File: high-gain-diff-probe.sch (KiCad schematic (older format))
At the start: 106 parts, among them J1 30V DC IN, J2 BNC, J4 BNC, J5 BNC, K1 FTR-B3SA012Z, K2 FTR-B3SA012Z, Q1 MMBT3906, SW1 MB04L1NCGD, SW2 MB05L1NCGD, SW3 SPDT, SW4 MB04L1NCGD, SW6 SPDT, U1 AD8428BRZ, U2 OP1177AR, U3 BUF634A, U6 LM393, U7 AD8671, U8 BUF634A

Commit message: Use larger thermal vias for cheaper PCBs
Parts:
- U3, U8: footprint Package_SO:SOIC-8-1EP_3.9x4.9mm_P1.27mm_EP2.41x3.81mm_ThermalVias -> high-gain-diff-probe:SOIC-8-1EP_3.9x4.9mm_P1.27mm_EP2.41x3.81mm_LargeThermalVias
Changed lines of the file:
@@
 F 0 "U3" H 14450 2550 50  0000 L CNN
 F 1 "BUF634A" H 14450 2150 50  0000 L CNN
-F 2 "Package_SO:SOIC-8-1EP_3.9x4.9mm_P1.27mm_EP2.41x3.81mm_ThermalVias" H 14350 2050 50  0001 C CNN
+F 2 "high-gain-diff-probe:SOIC-8-1EP_3.9x4.9mm_P1.27mm_EP2.41x3.81mm_LargeThermalVias" H 14350 2050 50  0001 C CNN
 F 3 "https://www.ti.com/lit/ds/symlink/buf634a.pdf?ts=1618584295467&ref_url=https%253A%252F%252Fcz.mouser.com%252F" H 14350 2350 50  0001 C CNN
 	1    14350 2350
@@
 F 0 "U8" H 4000 9150 50  0000 L CNN
 F 1 "BUF634A" H 4000 8850 50  0000 L CNN
-F 2 "Package_SO:SOIC-8-1EP_3.9x4.9mm_P1.27mm_EP2.41x3.81mm_ThermalVias" H 3950 8700 50  0001 C CNN
+F 2 "high-gain-diff-probe:SOIC-8-1EP_3.9x4.9mm_P1.27mm_EP2.41x3.81mm_LargeThermalVias" H 3950 8700 50  0001 C CNN
 F 3 "https://www.ti.com/lit/ds/symlink/buf634a.pdf?ts=1618584295467&ref_url=https%253A%252F%252Fcz.mouser.com%252F" H 3950 9000 50  0001 C CNN
 	1    3950 9000

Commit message: Add MPNs for everything else
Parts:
- D1, D2, D3: MPN (none) -> BAV199,215
- D17: value LED -> RED LED; footprint LED_THT:LED_D3.0mm -> LED_THT:LED_D5.0mm; MPN (none) -> MT4118-HR-A
- F4: value 1A Fast -> 500mA Fast; MPN (none) -> F0805B0R50FWTR
- J1: MPN (none) -> PJ-063AH
- J2, J4, J5: MPN (none) -> 0731385033
- Q1: MPN (none) -> MMBT3906-TP
- R10, R4, R5, R9: MPN (none) -> RT0603BRD071ML
- R13, R30: MPN (none) -> RMCF0603FT200R
- R14: MPN (none) -> CR0603-FX-1001ELF
- R15, R21: MPN (none) -> RT0603FRE07100KL
- R16: MPN (none) -> RMCF1210FT49R9
- R18, R19: MPN (none) -> WR06X1502FTL
- R2, R3: MPN (none) -> RMCF1210FT200R
- R24, R26: MPN (none) -> RMCF0603FT2K20
- R25: MPN (none) -> CR0603-FX-1002ELF
- R27: MPN (none) -> RMCF0603FT4K70
- R31: MPN (none) -> RMCF0603FT49R9
- U2: value OP1177AR -> OP1177; MPN (none) -> OP1177ARZ-REEL7
- U3, U8: MPN (none) -> BUF634AIDDAR
- U6: MPN (none) -> LM393PSR
- U7: MPN (none) -> AD8671ARZ-REEL7
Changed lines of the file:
@@
 F 2 "high-gain-diff-probe:SOIC-8-1EP_3.9x4.9mm_P1.27mm_EP2.41x3.81mm_LargeThermalVias" H 14350 2050 50  0001 C CNN
 F 3 "https://www.ti.com/lit/ds/symlink/buf634a.pdf?ts=1618584295467&ref_url=https%253A%252F%252Fcz.mouser.com%252F" H 14350 2350 50  0001 C CNN
+F 4 "BUF634AIDDAR" H 14350 2350 50  0001 C CNN "MPN"
 	1    14350 2350
 	1    0    0    -1
@@
 F 2 "Resistor_SMD:R_0603_1608Metric_Pad0.98x0.95mm_HandSolder" V 14290 4190 50  0001 C CNN
 F 3 "~" H 14250 4200 50  0001 C CNN
+F 4 "CR0603-FX-1001ELF" H 14250 4200 50  0001 C CNN "MPN"
 	1    14250 4200
 	-1   0    0    1
@@
 F 2 "Resistor_SMD:R_0603_1608Metric_Pad0.98x0.95mm_HandSolder" V 14290 4940 50  0001 C CNN
 F 3 "~" H 14250 4950 50  0001 C CNN
+F 4 "RT0603FRE07100KL" H 14250 4950 50  0001 C CNN "MPN"
 	1    14250 4950
 	-1   0    0    1
@@
 F 2 "Connector_Coaxial:BNC_Amphenol_B6252HB-NPP3G-50_Horizontal" H 900 2000 50  0001 C CNN
 F 3 " ~" H 900 2000 50  0001 C CNN
+F 4 "0731385033" H 900 2000 50  0001 C CNN "MPN"
 	1    900  2000
 	-1   0    0    -1
@@
 F 2 "Package_TO_SOT_SMD:SOT-23" H 8850 2350 50  0001 C CNN
 F 3 "~" H 8850 2350 50  0001 C CNN
+F 4 "BAV199,215" H 8850 2350 50  0001 C CNN "MPN"
 	1    8850 2350
 	1    0    0    1
@@
 F 2 "Resistor_SMD:R_0603_1608Metric_Pad0.98x0.95mm_HandSolder" V 12290 2340 50  0001 C CNN
 F 3 "~" H 12250 2350 50  0001 C CNN
+F 4 "RMCF0603FT200R" H 12250 2350 50  0001 C CNN "MPN"
 	1    12250 2350
 	0    1    1    0
@@
 F 2 "Resistor_SMD:R_1210_3225Metric_Pad1.30x2.65mm_HandSolder" V 14840 2340 50  0001 C CNN
 F 3 "~" H 14800 2350 50  0001 C CNN
+F 4 "RMCF1210FT49R9" H 14800 2350 50  0001 C CNN "MPN"
 	1    14800 2350
 	0    1    1    0
@@
 F 2 "Connector_Coaxial:BNC_Amphenol_B6252HB-NPP3G-50_Horizontal" H 15650 2350 50  0001 C CNN
 F 3 " ~" H 15650 2350 50  0001 C CNN
+F 4 "0731385033" H 15650 2350 50  0001 C CNN "MPN"
 	1    15650 2350
 	1    0    0    -1
@@
 F 2 "Resistor_SMD:R_1210_3225Metric_Pad1.30x2.65mm_HandSolder" V 1690 1990 50  0001 C CNN
 F 3 "~" H 1650 2000 50  0001 C CNN
+F 4 "RMCF1210FT200R" H 1650 2000 50  0001 C CNN "MPN"
 	1    1650 2000
 	0    1    1    0
@@
 F 2 "Resistor_SMD:R_1210_3225Metric_Pad1.30x2.65mm_HandSolder" V 1690 3790 50  0001 C CNN
 F 3 "~" H 1650 3800 50  0001 C CNN
+F 4 "RMCF1210FT200R" H 1650 3800 50  0001 C CNN "MPN"
 	1    1650 3800
 	0    1    1    0
@@
 F 2 "Resistor_SMD:R_0603_1608Metric_Pad0.98x0.95mm_HandSolder" V 3040 1140 50  0001 C CNN
 F 3 "~" H 3000 1150 50  0001 C CNN
+F 4 "RT0603BRD071ML" H 3000 1150 50  0001 C CNN "MPN"
 	1    3000 1150
 	0    -1   -1   0
@@
 F 2 "Resistor_SMD:R_0603_1608Metric_Pad0.98x0.95mm_HandSolder" V 3040 4690 50  0001 C CNN
 F 3 "~" H 3000 4700 50  0001 C CNN
+F 4 "RT0603BRD071ML" H 3000 4700 50  0001 C CNN "MPN"
 	1    3000 4700
 	0    -1   1    0
@@
 F 2 "Resistor_SMD:R_0603_1608Metric_Pad0.98x0.95mm_HandSolder" V 2940 3190 50  0001 C CNN
 F 3 "~" H 2900 3200 50  0001 C CNN
+F 4 "RT0603BRD071ML" H 2900 3200 50  0001 C CNN "MPN"
 	1    2900 3200
 	1    0    0    1
@@
 F 2 "Connector_Coaxial:BNC_Amphenol_B6252HB-NPP3G-50_Horizontal" H 950 3800 50  0001 C CNN
 F 3 " ~" H 950 3800 50  0001 C CNN
+F 4 "0731385033" H 950 3800 50  0001 C CNN "MPN"
 	1    950  3800
 	-1   0    0    -1
@@
 F 2 "Package_TO_SOT_SMD:SOT-23" H 8350 2350 50  0001 C CNN
 F 3 "~" H 8350 2350 50  0001 C CNN
+F 4 "BAV199,215" H 8350 2350 50  0001 C CNN "MPN"
 	1    8350 2350
 	0    1    -1   0
@@
 F 2 "Package_TO_SOT_SMD:SOT-23" H 9600 2350 50  0001 C CNN
 F 3 "~" H 9600 2350 50  0001 C CNN
+F 4 "BAV199,215" H 9600 2350 50  0001 C CNN "MPN"
 	1    9600 2350
 	0    1    -1   0
@@
 F 2 "Resistor_SMD:R_0603_1608Metric_Pad0.98x0.95mm_HandSolder" V 8840 4340 50  0001 C CNN
 F 3 "~" H 8800 4350 50  0001 C CNN
-F 4 "" H 8800 4350 50  0001 C CNN "MPN"
+F 4 "RMCF0603FT200R" H 8800 4350 50  0001 C CNN "MPN"
 	1    8800 4350
 	1    0    0    -1
@@
 F 2 "Resistor_SMD:R_0603_1608Metric_Pad0.98x0.95mm_HandSolder" V 9340 4740 50  0001 C CNN
 F 3 "~" H 9300 4750 50  0001 C CNN
-F 4 "" H 9300 4750 50  0001 C CNN "MPN"
+F 4 "RMCF0603FT49R9" H 9300 4750 50  0001 C CNN "MPN"
 	1    9300 4750
 	1    0    0    1
@@
 F 2 "Package_SO:SOIC-8_3.9x4.9mm_P1.27mm" H 13500 2250 50  0001 L CNN
 F 3 "http://www.ti.com/lit/ds/symlink/lmh6609.pdf" H 13750 2600 50  0001 C CNN
+F 4 "AD8671ARZ-REEL7" H 13600 2450 50  0001 C CNN "MPN"
 	1    13600 2450
 	1    0    0    -1
@@
 P 10100 8650
 F 0 "D17" V 10150 8500 50  0000 R CNN
-F 1 "LED" V 10050 8500 50  0000 R CNN
-F 2 "LED_THT:LED_D3.0mm" H 10100 8650 50  0001 C CNN
+F 1 "RED LED" V 10050 8500 50  0000 R CNN
+F 2 "LED_THT:LED_D5.0mm" H 10100 8650 50  0001 C CNN
 F 3 "~" H 10100 8650 50  0001 C CNN
 F 4 "Output Saturated" V 9950 8500 50  0000 R CNN "Name"
+F 5 "MT4118-HR-A" H 10100 8650 50  0001 C CNN "MPN"
 	1    10100 8650
 	0    -1   -1   0
@@
 F 2 "Resistor_SMD:R_0603_1608Metric_Pad0.98x0.95mm_HandSolder" V 10140 8340 50  0001 C CNN
 F 3 "~" H 10100 8350 50  0001 C CNN
+F 4 "RMCF0603FT4K70" H 10100 8350 50  0001 C CNN "MPN"
 	1    10100 8350
 	-1   0    0    1
@@
 F 2 "Resistor_SMD:R_0603_1608Metric_Pad0.98x0.95mm_HandSolder" V 9140 9240 50  0001 C CNN
 F 3 "~" H 9100 9250 50  0001 C CNN
+F 4 "CR0603-FX-1002ELF" H 9100 9250 50  0001 C CNN "MPN"
 	1    9100 9250
 	1    0    0    1
@@
 F 2 "Resistor_SMD:R_0603_1608Metric_Pad0.98x0.95mm_HandSolder" V 9140 8540 50  0001 C CNN
 F 3 "~" H 9100 8550 50  0001 C CNN
+F 4 "RMCF0603FT2K20" H 9100 8550 50  0001 C CNN "MPN"
 	1    9100 8550
 	1    0    0    1
@@
 F 2 "Resistor_SMD:R_0603_1608Metric_Pad0.98x0.95mm_HandSolder" V 9140 9890 50  0001 C CNN
 F 3 "~" H 9100 9900 50  0001 C CNN
+F 4 "RMCF0603FT2K20" H 9100 9900 50  0001 C CNN "MPN"
 	1    9100 9900
 	1    0    0    1
@@
 F 2 "Package_SO:SOIC-8_3.9x4.9mm_P1.27mm" H 11500 9100 50  0001 C CNN
 F 3 "http://www.ti.com/lit/ds/symlink/lm393.pdf" H 11500 9100 50  0001 C CNN
+F 4 "LM393PSR" H 11500 9100 50  0001 C CNN "MPN"
 	3    11500 9100
 	1    0    0    -1
@@
 F 2 "Package_SO:SOIC-8_3.9x4.9mm_P1.27mm" H 9700 9550 50  0001 C CNN
 F 3 "http://www.ti.com/lit/ds/symlink/lm393.pdf" H 9700 9550 50  0001 C CNN
+F 4 "LM393PSR" H 9700 9550 50  0001 C CNN "MPN"
 	2    9700 9550
 	1    0    0    1
@@
 F 2 "Package_SO:SOIC-8_3.9x4.9mm_P1.27mm" H 9700 8900 50  0001 C CNN
 F 3 "http://www.ti.com/lit/ds/symlink/lm393.pdf" H 9700 8900 50  0001 C CNN
+F 4 "LM393PSR" H 9700 8900 50  0001 C CNN "MPN"
 	1    9700 8900
 	1    0    0    1
@@
 P 12550 4650
 F 0 "U2" H 12750 4950 50  0000 C CNN
-F 1 "OP1177AR" H 12750 4850 50  0000 C CNN
+F 1 "OP1177" H 12750 4850 50  0000 C CNN
 F 2 "Package_SO:SOIC-8_3.9x4.9mm_P1.27mm" H 12550 4350 50  0001 C CNN
 F 3 "https://www.analog.com/media/en/technical-documentation/data-sheets/OP1177_2177_4177.pdf" H 12550 4650 50  0001 C CNN
+F 4 "OP1177ARZ-REEL7" H 12550 4650 50  0001 C CNN "MPN"
 	1    12550 4650
 	-1   0    0    -1
@@
 F 2 "Resistor_SMD:R_0603_1608Metric_Pad0.98x0.95mm_HandSolder" V 2940 2590 50  0001 C CNN
 F 3 "~" H 2900 2600 50  0001 C CNN
+F 4 "RT0603BRD071ML" H 2900 2600 50  0001 C CNN "MPN"
 	1    2900 2600
 	1    0    0    -1
@@
 F 2 "Package_TO_SOT_SMD:SOT-23" H 7250 4125 50  0001 L CIN
 F 3 "https://www.onsemi.com/pub/Collateral/2N3906-D.PDF" H 7050 4200 50  0001 L CNN
+F 4 "MMBT3906-TP" H 7050 4200 50  0001 C CNN "MPN"
 	1    7050 4200
 	-1   0    0    1
@@
 F 2 "Resistor_SMD:R_0603_1608Metric_Pad0.98x0.95mm_HandSolder" V 7440 4190 50  0001 C CNN
 F 3 "~" H 7400 4200 50  0001 C CNN
+F 4 "RT0603FRE07100KL" H 7400 4200 50  0001 C CNN "MPN"
 	1    7400 4200
 	0    1    1    0
@@
 P 2000 8200
 F 0 "F4" V 1803 8200 50  0000 C CNN
-F 1 "1A Fast" V 1894 8200 50  0000 C CNN
+F 1 "500mA Fast" V 1894 8200 50  0000 C CNN
 F 2 "Fuse:Fuse_0805_2012Metric_Pad1.15x1.40mm_HandSolder" V 1930 8200 50  0001 C CNN
 F 3 "~" H 2000 8200 50  0001 C CNN
+F 4 "F0805B0R50FWTR" H 2000 8200 50  0001 C CNN "MPN"
 	1    2000 8200
 	0    1    1    0
@@
 F 2 "Connector_BarrelJack:BarrelJack_CUI_PJ-063AH_Horizontal" H 1600 8260 50  0001 C CNN
 F 3 "~" H 1600 8260 50  0001 C CNN
+F 4 "PJ-063AH" H 1550 8300 50  0001 C CNN "MPN"
 	1    1550 8300
 	1    0    0    -1
@@
 F 2 "Resistor_SMD:R_0603_1608Metric_Pad0.98x0.95mm_HandSolder" V 3490 9340 50  0001 C CNN
 F 3 "~" H 3450 9350 50  0001 C CNN
+F 4 "WR06X1502FTL" H 3450 9350 50  0001 C CNN "MPN"
 	1    3450 9350
 	1    0    0    -1
@@
 F 2 "Resistor_SMD:R_0603_1608Metric_Pad0.98x0.95mm_HandSolder" V 3490 8640 50  0001 C CNN
 F 3 "~" H 3450 8650 50  0001 C CNN
+F 4 "WR06X1502FTL" H 3450 8650 50  0001 C CNN "MPN"
 	1    3450 8650
 	1    0    0    -1
@@
 F 2 "high-gain-diff-probe:SOIC-8-1EP_3.9x4.9mm_P1.27mm_EP2.41x3.81mm_LargeThermalVias" H 3950 8700 50  0001 C CNN
 F 3 "https://www.ti.com/lit/ds/symlink/buf634a.pdf?ts=1618584295467&ref_url=https%253A%252F%252Fcz.mouser.com%252F" H 3950 9000 50  0001 C CNN
+F 4 "BUF634AIDDAR" H 3950 9000 50  0001 C CNN "MPN"
 	1    3950 9000
 	1    0    0    -1

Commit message: Tweak layout
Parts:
- D4, D5, D6: footprint Diode_SMD:D_SOD-123F -> Diode_SMD:D_SOD-123
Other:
- moved on the sheet: C1, C10, C11, C12, C13, C14, C16, C17, C18, C19, C2, C20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

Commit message: Fix 10K MPN
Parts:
- R22, R23, R7, R8: MPN ERA-3AEB5232V -> RT0603BRD1010KL
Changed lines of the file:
@@
 F 2 "Resistor_SMD:R_0603_1608Metric_Pad0.98x0.95mm_HandSolder" V 6090 3440 50  0001 C CNN
 F 3 "~" H 6050 3450 50  0001 C CNN
-F 4 "ERA-3AEB5232V" H 6050 3450 50  0001 C CNN "MPN"
+F 4 "RT0603BRD1010KL" H 6050 3450 50  0001 C CNN "MPN"
 	1    6050 3450
 	1    0    0    -1
@@
 F 2 "Resistor_SMD:R_0603_1608Metric_Pad0.98x0.95mm_HandSolder" V 6090 2840 50  0001 C CNN
 F 3 "~" H 6050 2850 50  0001 C CNN
-F 4 "ERA-3AEB5232V" H 6050 2850 50  0001 C CNN "MPN"
+F 4 "RT0603BRD1010KL" H 6050 2850 50  0001 C CNN "MPN"
 	1    6050 2850
 	1    0    0    -1
@@
 F 2 "Resistor_SMD:R_0603_1608Metric_Pad0.98x0.95mm_HandSolder" V 14890 4590 50  0001 C CNN
 F 3 "~" H 14850 4600 50  0001 C CNN
-F 4 "ERA-3AEB5232V" H 14850 4600 50  0001 C CNN "MPN"
+F 4 "RT0603BRD1010KL" H 14850 4600 50  0001 C CNN "MPN"
 	1    14850 4600
 	1    0    0    -1
@@
 F 2 "Resistor_SMD:R_0603_1608Metric_Pad0.98x0.95mm_HandSolder" V 14890 5190 50  0001 C CNN
 F 3 "~" H 14850 5200 50  0001 C CNN
-F 4 "ERA-3AEB5232V" H 14850 5200 50  0001 C CNN "MPN"
+F 4 "RT0603BRD1010KL" H 14850 5200 50  0001 C CNN "MPN"
 	1    14850 5200
 	1    0    0    -1

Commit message: Begin work on new version with no relays and manual attenuator switching
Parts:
- removed D5, D6: DSS15, Diode_SMD:D_SOD-123, symbol Device:D_Schottky
- removed K1, K2: FTR-B3SA012Z, Relay_SMD:Relay_Fujitsu_FTR-B3S, symbol Relay:G6K-2
- removed Q1: MMBT3906, Package_TO_SOT_SMD:SOT-23, symbol Transistor_BJT:MMBT3906
- removed R20: 1k 1/4W, Resistor_SMD:R_1206_3216Metric_Pad1.30x1.75mm_HandSolder, symbol Device:R_US
- removed R21: 100k, Resistor_SMD:R_0603_1608Metric_Pad0.98x0.95mm_HandSolder, symbol Device:R_US
- removed SW1, SW4: MB04L1NCGD, high-gain-diff-probe:SW_DPNT_CK_M, symbol high-gain-diff-probe:SW_DP5T
- removed SW2: MB05L1NCGD, high-gain-diff-probe:SW_DPNT_CK_M, symbol high-gain-diff-probe:SW_DP5T
- added JP3, JP4: TERM, Connector_PinHeader_2.54mm:PinHeader_1x03_P2.54mm_Vertical, symbol Device:Jumper_NC_Small
- added SW1, SW2, SW4: DP3T, high-gain-diff-probe:SW_NKK_MRB24B, symbol high-gain-diff-probe:SW_DP3T_NKK_MRB
- added SW5, SW7: DP3T, high-gain-diff-probe:SW_TE_1825263-2_DPDT, symbol Switch:SW_DPDT_x2
- C3, C4: value 1uF 100V FILM -> 1uF 100V
- SW3: Name Low Pass Enable -> Low Pass
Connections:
- net labels added: RG_2000X
- net labels removed: ATTEN_EN
- wire segments 364 -> 315
- no-connect marks 7 -> 4
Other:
- note removed: "0.1X"
- note removed: "100X"
- note removed: "10X"
- note removed: "1X"
- note removed: "2 12V relays in series to run off\nthe 30V input through a resistor."
- note removed: "2000X"
- note removed: "Enable 100:1 Attenuator\nfor 10X and 0.1X ranges."
- moved on the sheet: C1, C10, C11, C12, C13, C14, C16, C17, C18, C19, C2, C20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

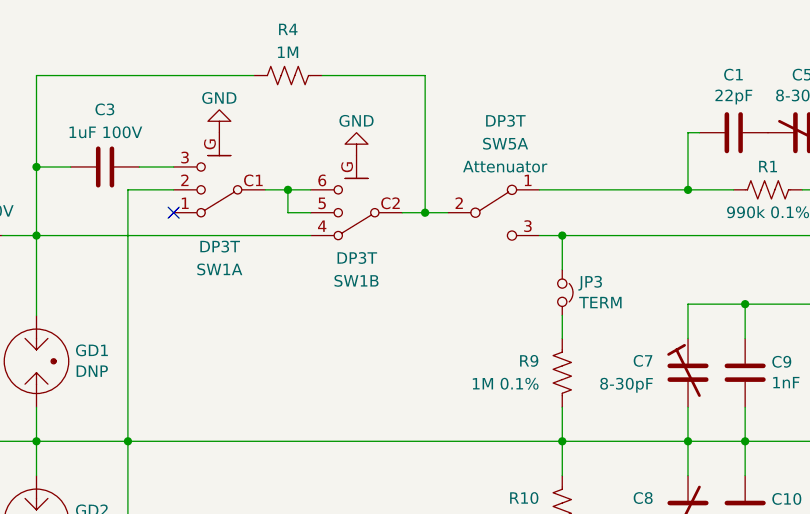
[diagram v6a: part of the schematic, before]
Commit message: Complete major layout of no-relay design
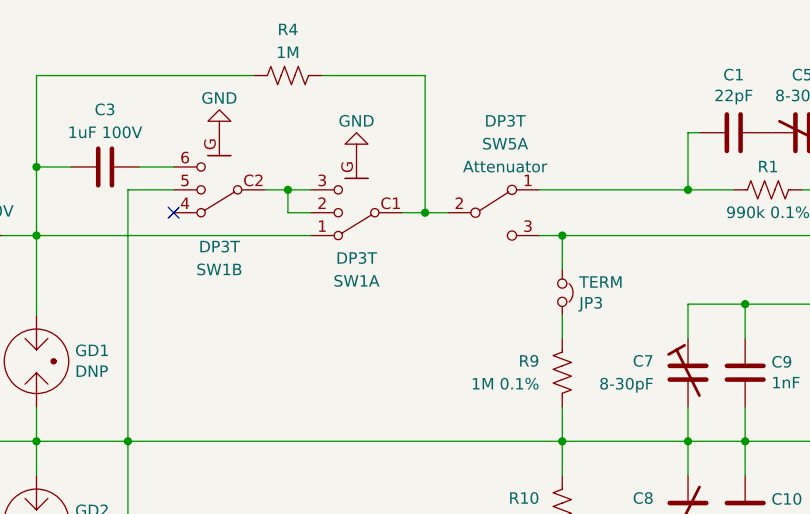
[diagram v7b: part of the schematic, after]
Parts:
- F1, F2: footprint high-gain-diff-probe:Fuseholder_Schurter_0031.8273 -> Fuse:Fuseholder_Cylinder-5x20mm_Schurter_FAB_0031-355x_Horizontal_Closed; MPN 0031.8273 -> (none)
- R2, R3: footprint Resistor_SMD:R_1210_3225Metric_Pad1.30x2.65mm_HandSolder -> Resistor_SMD:R_MiniMELF_MMA-0204; MPN RMCF1210FT200R -> SMA-A0204BTNX180R
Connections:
- net GND: now also SW1.5; no longer SW1.2 (5)
- net at C3.1: now also SW1.6; no longer SW1.3 (6)
- net at C3.2, F1.1, GD1.3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: now also SW1.1 (4); no longer SW1.4
- net at R9.1: now also JP3.1; no longer JP3.2
- net at R4.2, SW5.2 (B): now also SW1.C1 (C2); no longer SW1.C2
- net at SW5.3 (C), SW5.6 (C): now also JP3.2; no longer JP3.1
- new net: SW1.2 (5), SW1.3 (6), SW1.C2

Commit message: Layout Tweaks
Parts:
- D17: MPN MT4118-HR-A -> 151051RS11000
- SW3: symbol Switch:SW_DPDT_x2 -> high-gain-diff-probe:SW_DPDT_x2_GND
- SW5, SW7: value DP3T -> DPDT; symbol Switch:SW_DPDT_x2 -> high-gain-diff-probe:SW_DPDT_x2_GND
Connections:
- net GND: now also SW3.G, SW5.G, SW5.G, SW7.G, SW7.G
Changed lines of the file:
@@
 $EndComp
 $Comp
-L Switch:SW_DPDT_x2 SW5
+L high-gain-diff-probe:SW_DPDT_x2_GND SW5
 U 2 1 629BDA53
 P 6300 1700
-F 0 "SW5" H 6350 2000 50  0000 C CNN
-F 1 "DP3T" H 6350 2100 50  0000 C CNN
+F 0 "SW5" H 6350 2100 50  0000 C CNN
+F 1 "DPDT" H 6350 2000 50  0000 C CNN
 F 2 "high-gain-diff-probe:SW_TE_1825263-2_DPDT" H 6300 1700 50  0001 C CNN
 F 3 "~" H 6300 1700 50  0001 C CNN
@@
 $EndComp
 $Comp
-L Switch:SW_DPDT_x2 SW5
+L high-gain-diff-probe:SW_DPDT_x2_GND SW5
 U 1 1 628E4D9B
 P 4350 1700
-F 0 "SW5" H 4400 2000 50  0000 C CNN
-F 1 "DP3T" H 4400 2100 50  0000 C CNN
+F 0 "SW5" H 4400 2100 50  0000 C CNN
+F 1 "DPDT" H 4400 2000 50  0000 C CNN
 F 2 "high-gain-diff-probe:SW_TE_1825263-2_DPDT" H 4350 1700 50  0001 C CNN
 F 3 "~" H 4350 1700 50  0001 C CNN
@@
 $EndComp
 $Comp
-L Switch:SW_DPDT_x2 SW7
+L high-gain-diff-probe:SW_DPDT_x2_GND SW7
 U 2 1 622D9945
 P 6300 3700
-F 0 "SW7" H 6300 3300 50  0000 C CNN
-F 1 "DP3T" H 6300 3400 50  0000 C CNN
+F 0 "SW7" H 6300 4150 50  0000 C CNN
+F 1 "DPDT" H 6300 4050 50  0000 C CNN
 F 2 "high-gain-diff-probe:SW_TE_1825263-2_DPDT" H 6300 3700 50  0001 C CNN
 F 3 "~" H 6300 3700 50  0001 C CNN
-F 4 "Attenuator" H 6300 3500 50  0000 C CNN "Name"
+F 4 "Attenuator" H 6300 3950 50  0000 C CNN "Name"
 F 5 "1825263-2" V 6300 3700 50  0001 C CNN "MPN"
 	2    6300 3700
@@
 $EndComp
 $Comp
-L Switch:SW_DPDT_x2 SW7
+L high-gain-diff-probe:SW_DPDT_x2_GND SW7
 U 1 1 62077799
 P 4350 3700
-F 0 "SW7" H 4350 3300 50  0000 C CNN
-F 1 "DP3T" H 4350 3400 50  0000 C CNN
+F 0 "SW7" H 4350 4150 50  0000 C CNN
+F 1 "DPDT" H 4350 4050 50  0000 C CNN
 F 2 "high-gain-diff-probe:SW_TE_1825263-2_DPDT" H 4350 3700 50  0001 C CNN
 F 3 "~" H 4350 3700 50  0001 C CNN
-F 4 "Attenuator" H 4350 3500 50  0000 C CNN "Name"
+F 4 "Attenuator" H 4350 3950 50  0000 C CNN "Name"
 F 5 "1825263-2" V 4350 3700 50  0001 C CNN "MPN"
 	1    4350 3700
@@
 F 3 "~" H 10000 8500 50  0001 C CNN
 F 4 "Output Saturated" V 9850 8350 50  0000 R CNN "Name"
-F 5 "MT4118-HR-A" H 10000 8500 50  0001 C CNN "MPN"
+F 5 "151051RS11000" H 10000 8500 50  0001 C CNN "MPN"
 	1    10000 8500
 	0    -1   -1   0
@@
 $EndComp
 $Comp
-L Switch:SW_DPDT_x2 SW3
+L high-gain-diff-probe:SW_DPDT_x2_GND SW3
 U 1 1 60F99B6D
 P 12750 3400
@@
 	0    1    1    0
 $EndComp
+$Comp
+L power:GND #PWR0123
+U 1 1 60D36F6C
+P 6300 1950
+F 0 "#PWR0123" H 6300 1700 50  0001 C CNN
+F 1 "GND" H 6300 1800 50  0000 C CNN
+F 2 "" H 6300 1950 50  0001 C CNN
+F 3 "" H 6300 1950 50  0001 C CNN
+	1    6300 1950
+	1    0    0    -1
+$EndComp
+$Comp
+L power:GND #PWR0124
+U 1 1 60D379D3
+P 4350 1950
+F 0 "#PWR0124" H 4350 1700 50  0001 C CNN
+F 1 "GND" H 4350 1800 50  0000 C CNN
+F 2 "" H 4350 1950 50  0001 C CNN
+F 3 "" H 4350 1950 50  0001 C CNN
+	1    4350 1950
+	1    0    0    -1
+$EndComp
+$Comp
+L power:GND #PWR0125
+U 1 1 60D3643C
+P 4350 3450
+F 0 "#PWR0125" H 4350 3200 50  0001 C CNN
+F 1 "GND" H 4350 3300 50  0000 C CNN
+F 2 "" H 4350 3450 50  0001 C CNN
+F 3 "" H 4350 3450 50  0001 C CNN
+	1    4350 3450
+	-1   0    0    1
+$EndComp
+Wire Wire Line
+	13000 3400 13050 3400
+Wire Wire Line
+	13050 3400 13050 3450
+$Comp
+L power:GND #PWR0126
+U 1 1 60D5CACA
+P 13050 3450
+F 0 "#PWR0126" H 13050 3200 50  0001 C CNN
+F 1 "GND" H 13050 3300 50  0000 C CNN
+F 2 "" H 13050 3450 50  0001 C CNN
+F 3 "" H 13050 3450 50  0001 C CNN
+	1    13050 3450
+	1    0    0    -1
+$EndComp
+$Comp
+L power:GND #PWR0122
+U 1 1 60D369BC
+P 6300 3450
+F 0 "#PWR0122" H 6300 3200 50  0001 C CNN
+F 1 "GND" H 6300 3300 50  0000 C CNN
+F 2 "" H 6300 3450 50  0001 C CNN
+F 3 "" H 6300 3450 50  0001 C CNN
+	1    6300 3450
+	-1   0    0    1
+$EndComp
 $EndSCHEMATC
